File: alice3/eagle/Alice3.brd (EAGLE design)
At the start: 100 x 80 mm, 14 parts, among them IC1 27C512, IC2 128k x 8 RAM, IC3 Z80, IC4 GAL22V10, IC5 i8259

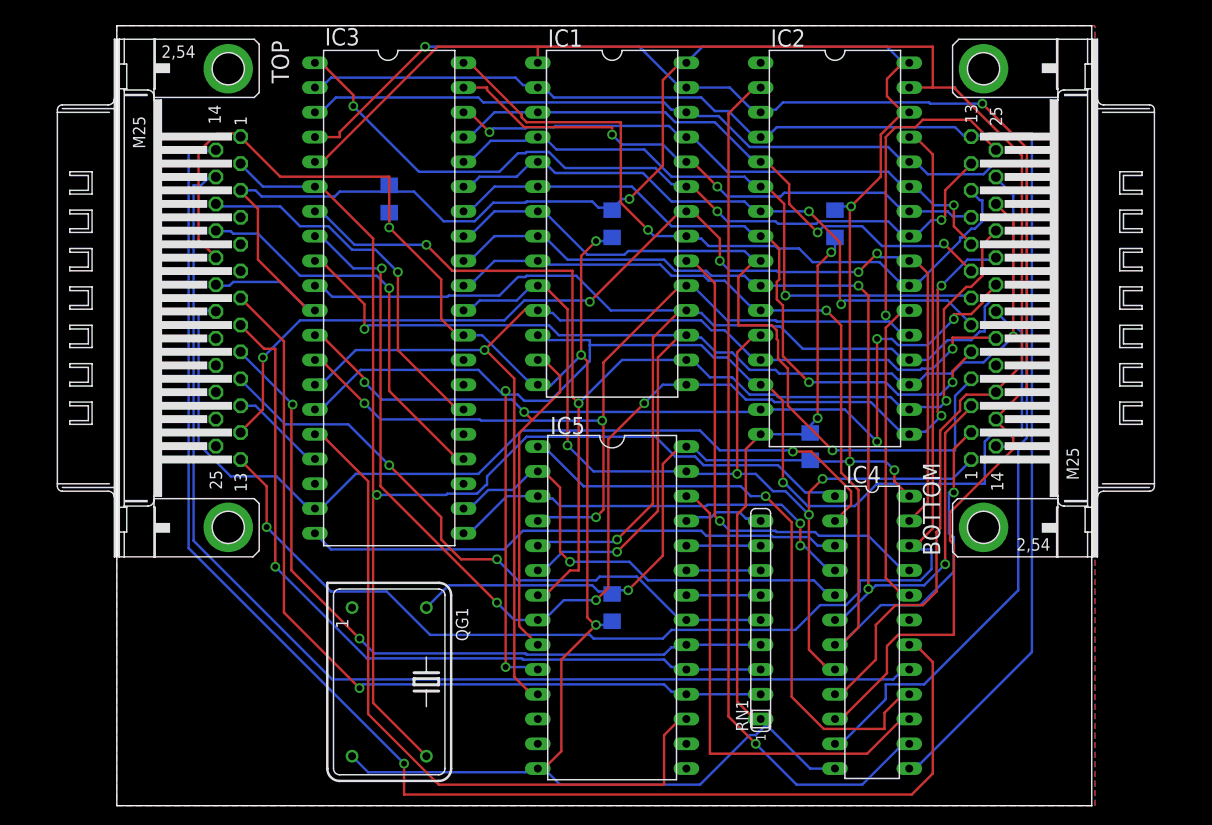
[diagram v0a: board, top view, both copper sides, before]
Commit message: New version - Added '*' to active-low signal names (e.g. RESET*) - Connected RESET* and M1 to GAL - More decoupling caps! - Moved some components around on PCB - Remove unused .pro file
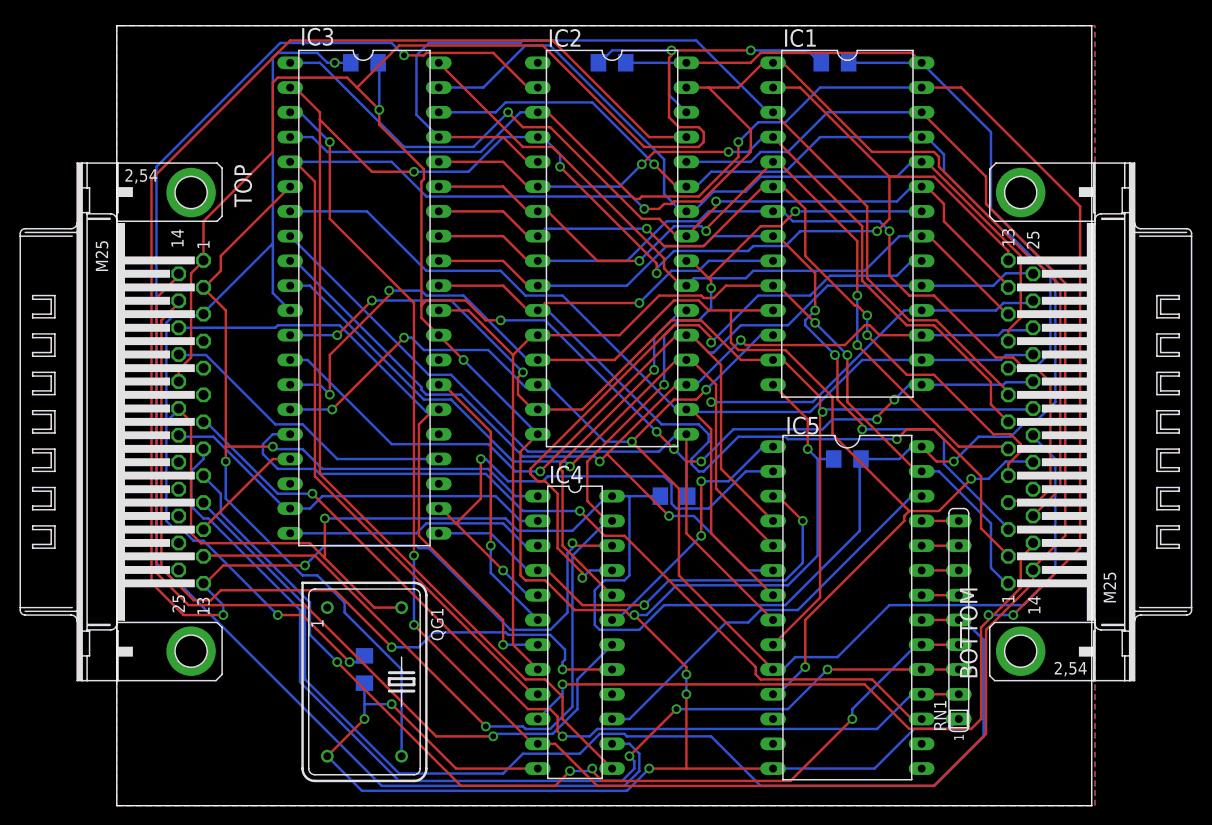
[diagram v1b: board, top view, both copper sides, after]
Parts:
- added C6: 0.1uF, resistor:C1206
- moved IC4 30.5 mm to (47.0, 17.8)
- moved IC1 24.1 mm to (74.9, 59.7)
- moved IC5 24.1 mm to (74.9, 20.3)
- moved IC2 22.9 mm to (50.8, 57.1)
- moved RN1 20.3 mm to (86.4, 19.1)
- moved C2 16.5 mm to (50.8, 76.2), turned to 0 degrees
- moved C4 16.5 mm to (73.7, 76.2), turned to 0 degrees
- moved C1 14.2 mm to (25.4, 76.2), turned to 180 degrees
- moved BOTTOM 13.3 mm to (92.7, 39.4)
- moved TOP 13.3 mm to (7.62, 39.4)
- moved C3 13.1 mm to (57.1, 31.8), turned to 180 degrees
- moved C5 4.02 mm to (74.9, 35.6), turned to 0 degrees
- moved IC3 2.54 mm to (25.4, 52.1)
- moved QG1 2.54 mm to (25.4, 12.7)
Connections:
- net BUSAK renamed BUSAK*
- net BUSRQ renamed BUSRQ*
- net INT renamed INT*
- net IRQ_CLR* renamed INTA*
- removed net M1: IC3.27
- removed net RESET: IC3.26, TOP.16
- new net M1*: IC3.27, IC4.6
- new net RESET*: IC3.26, IC4.7, TOP.16
- net A1: no longer IC4.7
- net A2: no longer IC4.6
- net CS_8259*: now also IC4.19; no longer IC4.16
- net GND: now also C6.2
- net VCC: now also C6.1
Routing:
- net GND: track 249.3 -> 396.0 mm, vias 6 -> 14
- net VCC: track 227.2 -> 341.0 mm
- net A13: track 149.8 -> 225.6 mm, vias 0 -> 3
- net RESET*: track 0.00 -> 63.0 mm, vias 0 -> 1
- net BANK: track 89.4 -> 151.7 mm
- net A14: track 155.1 -> 215.5 mm, vias 2 -> 4
- net IO_R*: track 148.1 -> 91.0 mm
- net IRQ3: track 65.3 -> 119.1 mm, vias 2 -> 0
- net MREQ*: track 95.0 -> 41.6 mm, vias 1 -> 0
- net A12: track 148.3 -> 193.2 mm, vias 0 -> 4
- net A15: track 156.1 -> 200.0 mm, vias 0 -> 1
- net MEM_W*: track 134.0 -> 174.1 mm, vias 1 -> 3
- net A7: track 61.8 -> 101.4 mm, vias 2 -> 0
- net RESET: track 39.1 -> 0.00 mm, vias 1 -> 0
- net IO_W*: track 118.9 -> 82.3 mm, vias 0 -> 2
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- added copper zone on layer 1, net N$100
- added copper zone on layer 16, net N$200
- removed copper zone on layer 16, net N$2
- removed copper zone on layer 1, net N$3
